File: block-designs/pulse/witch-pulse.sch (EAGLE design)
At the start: 17 parts, among them IC1 4002N, IC3 74HC160N, IC4 4511N

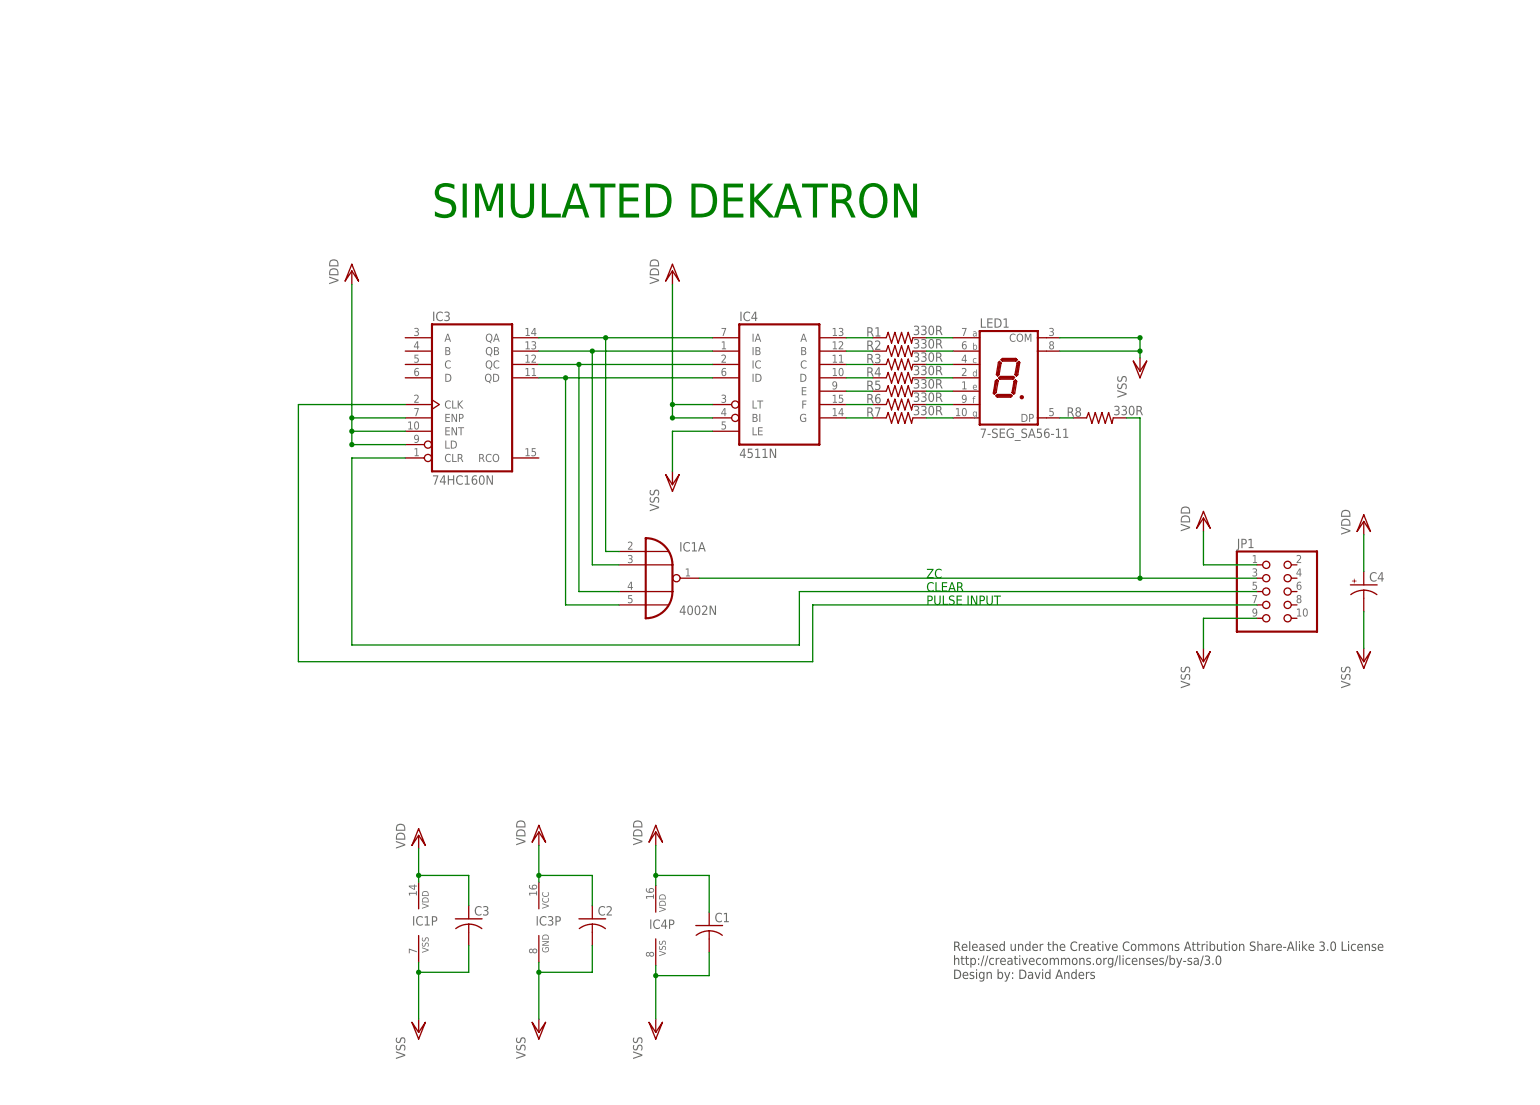
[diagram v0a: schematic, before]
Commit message: updated schematics and layouts for phase 1 block designs
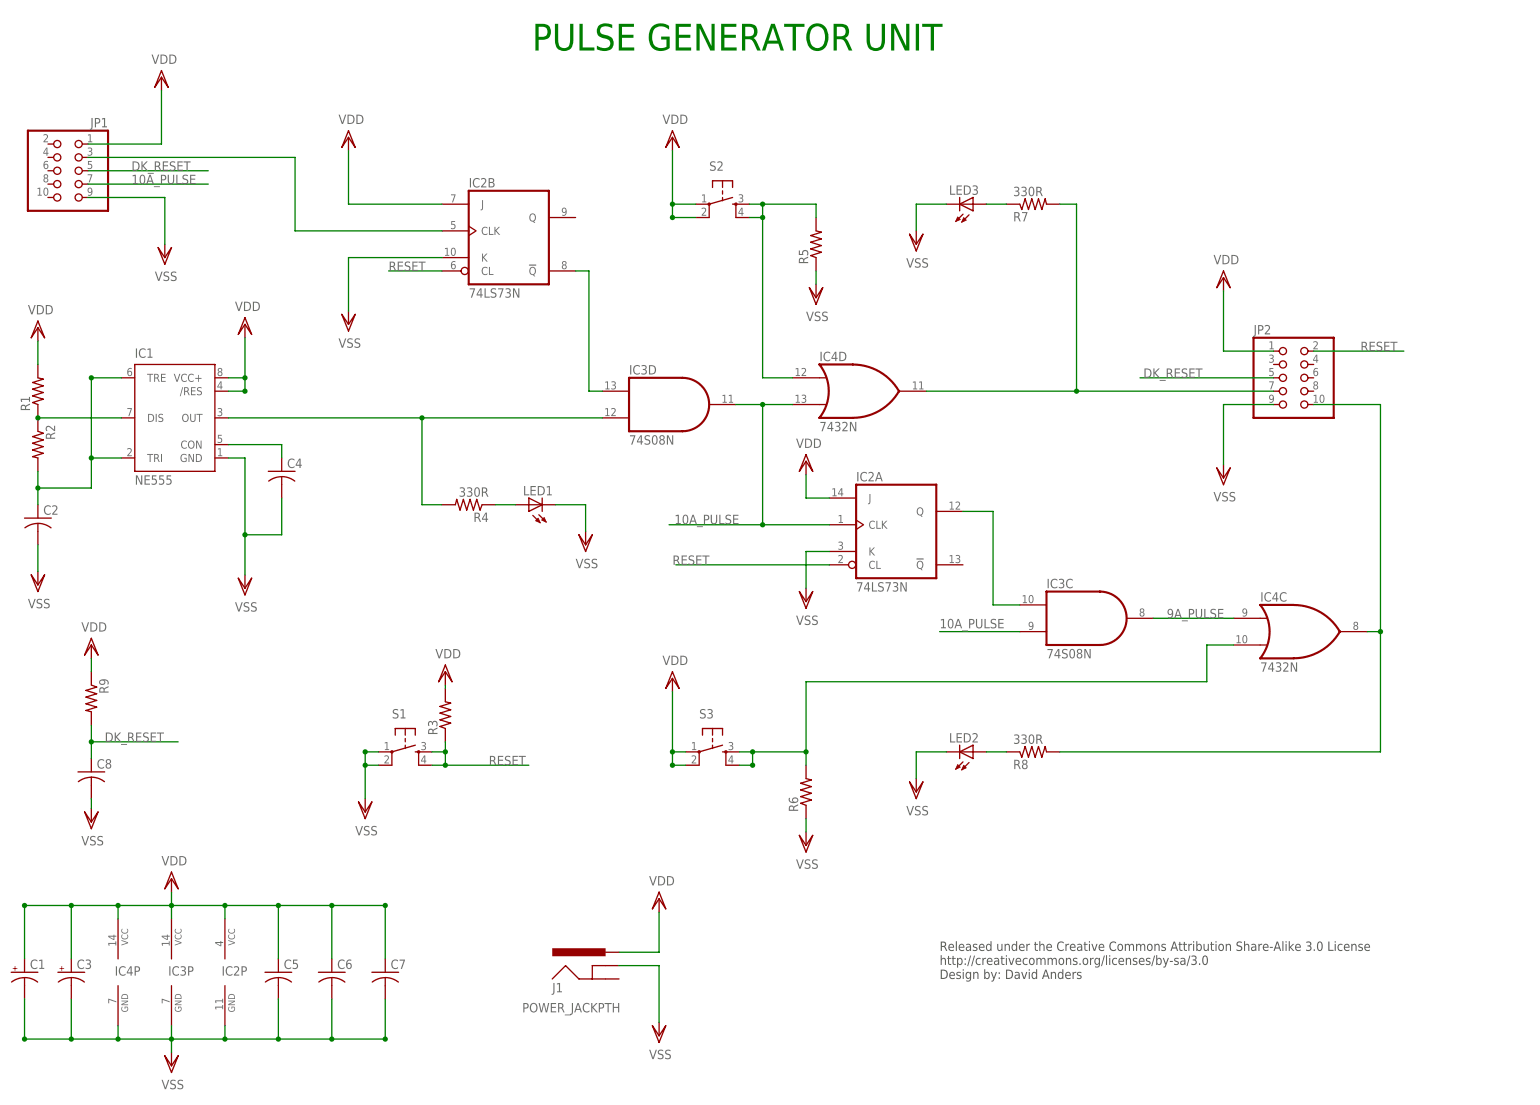
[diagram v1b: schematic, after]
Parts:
- added C5, C6, C7: (no value), resistor:C-US025-025X050
- added C8: (no value), resistor:C-US025-040X050
- added IC2: 74LS73N, 74xx-us:74LS73N
- added J1: POWER_JACKPTH, SparkFun-Connectors:POWER_JACKPTH
- added JP2: (no value), pinhead:PINHD-2X5
- added LED2, LED3: (no value), SparkFun-LED:LED5MM
- added R9: (no value), resistor:R-US_0204/5
- added S1, S2, S3: (no value), SparkFun-Electromechanical:TAC_SWITCHPTH
- C1, C3: device resistor:C-US025-025X050 -> resistor:CPOL-USE2.5-5
- C2: device resistor:C-US025-025X050 -> resistor:C-US025-040X050
- C4: device resistor:CPOL-USE2-5 -> resistor:C-US025-025X050
- IC1: value 4002N -> NE555; device 40xx:4002N -> st-microelectronics:NE555
- IC3: value 74HC160N -> 74S08N; device 74xx-eu:74HC160N -> 74xx-us:74S08N
- IC4: value 4511N -> 7432N; device 45xx:4511N -> 74xx-us:7432N
- LED1: value 7-SEG_SA56-11 -> (none); device display-kingbright:7-SEG_SA56-11 -> SparkFun-LED:LED5MM
- R1, R2, R3, R5, R6: value 330R -> (none)
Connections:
- removed net N$1: IC1A.O, JP1.3, R8.2
- removed net N$11: IC1A.I1, IC3A.QB, IC4A.IB
- removed net N$16: LED1.C, R3.2
- removed net N$20: LED1.G, R7.2
- removed net N$21: LED1.DP, R8.1
- removed net N$25: IC3A.CLK, JP1.7
- removed net N$3: IC4A.A, R1.1
- removed net N$8: IC4A.F, R6.1
- new net 10A_PULSE: IC2A.CLK, IC3C.I0, IC3D.O, IC4D.I1, JP1.7
- new net 9A_PULSE: IC3C.O, IC4C.I0
- new net DK_RESET: C8.1, JP1.5, JP2.5, R9.2
- new net RESET: IC2A.CL, IC2B.CL, JP2.2, R3.1, S1.3, S1.4
- net N$10: now also IC1.DIS, R1.1, R2.1; no longer IC1A.I0, IC3A.QA, IC4A.IA
- net N$12: now also IC2B.CLK, JP1.3; no longer IC1A.I2, IC3A.QC, IC4A.IC
- net N$13: now also C2.1, IC1.TRE, IC1.TRI, R2.2; no longer IC1A.I3, IC3A.QD, IC4A.ID
- net N$14: now also C4.1, IC1.CON; no longer LED1.A, R1.2
- net N$15: now also LED1.A, R4.1; no longer LED1.B, R2.2
- net N$17: now also LED3.A, R7.1; no longer LED1.D, R4.2
- net N$18: now also LED2.A, R8.1; no longer LED1.E, R5.2
- net N$19: now also IC4D.O, JP2.7, R7.2; no longer LED1.F, R6.2
- net N$2: now also IC1.OUT, IC3D.I0, R4.2; no longer IC3A.CLR, JP1.5
- net N$4: now also IC4C.O, JP2.10, R8.2; no longer IC4A.B, R2.1
- net N$5: now also IC2B.!Q, IC3D.I1; no longer IC4A.C, R3.1
- net N$6: now also IC4D.I0, R5.2, S2.3, S2.4; no longer IC4A.D, R4.1
- net N$7: now also IC2A.Q, IC3C.I1; no longer IC4A.E, R5.1
- net N$9: now also IC4C.I1, R6.2, S3.3, S3.4; no longer IC4A.G, R7.1
- net VDD: now also C1.+, C3.+, C5.1, C6.1, C7.1, IC1./RES, IC1.VCC+, IC2A.J, IC2B.J, IC2P.VCC, IC4P.VCC, J1.PWR, JP2.1, R1.2, R3.2, R9.1, S2.1, S2.2, S3.1, S3.2; no longer C1.1, C2.1, C3.1, C4.+, IC1P.VDD, IC3A.ENP, IC3A.ENT, IC3A.LD, IC4A.BI, IC4A.LT, IC4P.VDD
- net VSS: now also C1.-, C3.-, C4.2, C5.2, C6.2, C7.2, C8.2, IC1.GND, IC2A.K, IC2B.K, IC2P.GND, IC4P.GND, J1.GNDBREAK, JP2.9, LED1.C, LED2.C, LED3.C, R5.1, R6.1, S1.1, S1.2; no longer C1.2, C3.2, C4.-, IC1P.VSS, IC4A.LE, IC4P.VSS, LED1.COM@1, LED1.COM@2
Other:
- note added: "PULSE GENERATOR UNIT"
- note removed: "CLEAR"
- note removed: "PULSE INPUT"
- note removed: "SIMULATED DEKATRON"
- note removed: "ZC"
- moved on the sheet: C2, IC3P, IC4P, JP1, R1, R2, R3, R4, R5, R6, R7, R8
